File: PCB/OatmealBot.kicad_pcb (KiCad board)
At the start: 2 copper layers, 65 x 56 mm, 43 parts, among them J1 4, J10 3, J11 6, J12 7, J2 RPi_GPIO, J3 5, J4 1, J5 3, J6 4, J7 2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

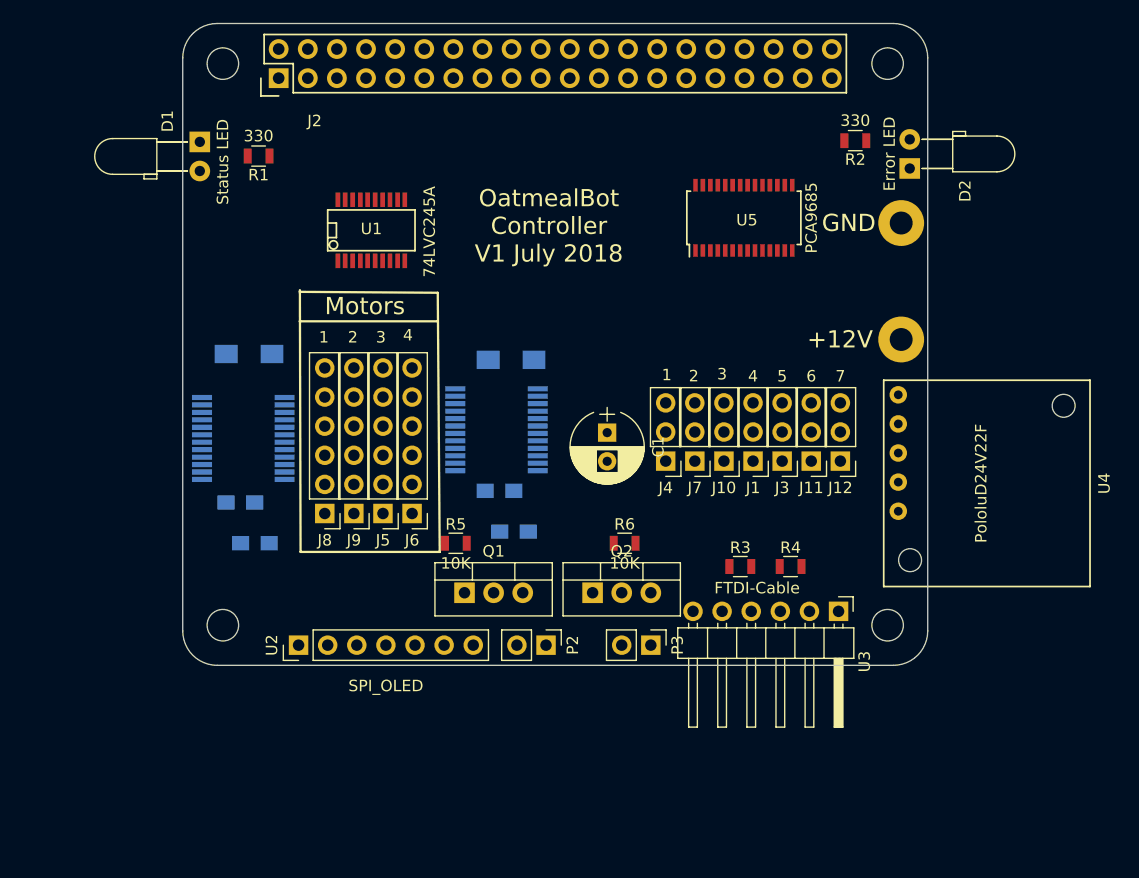
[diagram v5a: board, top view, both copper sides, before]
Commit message: PCB layout changes
Move things around to make the high power tracks shorter
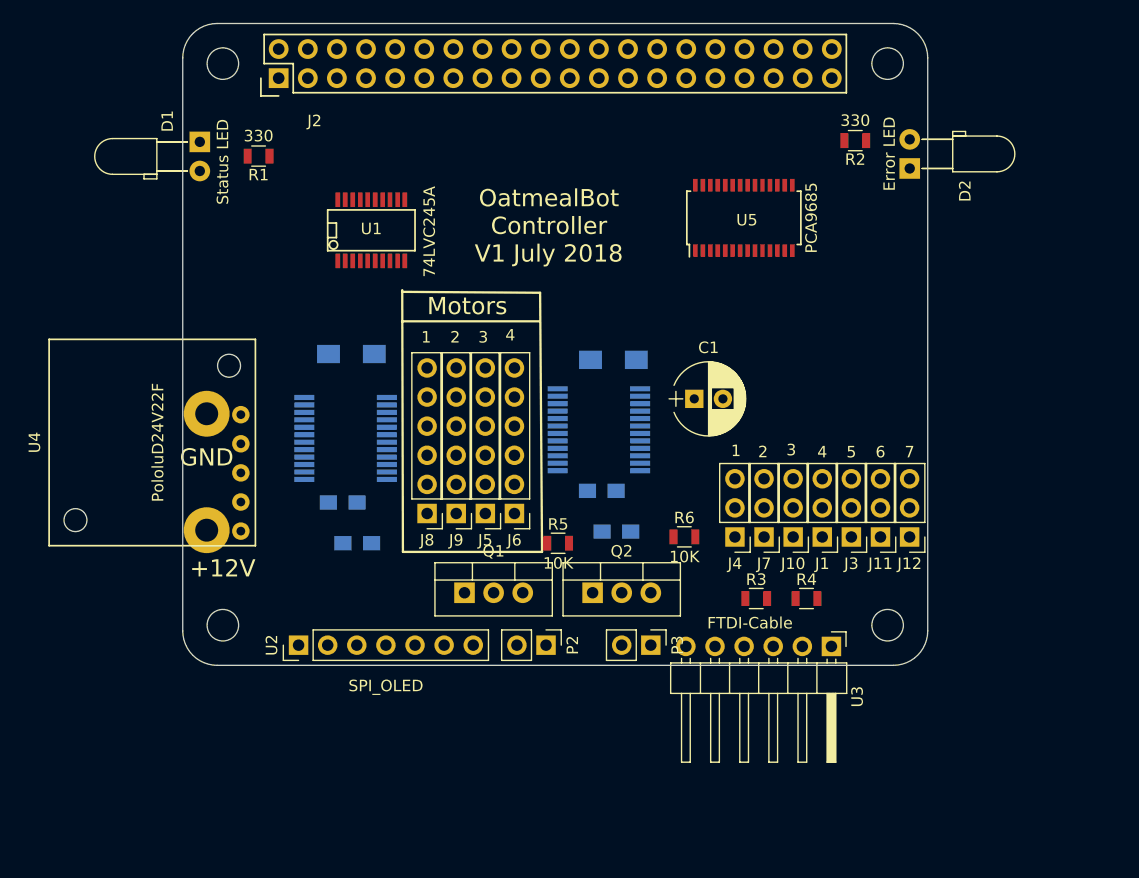
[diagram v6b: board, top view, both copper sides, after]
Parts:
- moved U4 72.9 mm to (9.84, 61.1), turned to 270 degrees
- moved P1 62.8 mm to (14.6, 58.5)
- moved J11 8.96 mm to (73.4, 69.3)
- moved J12 8.96 mm to (75.9, 69.3)
- moved J7 8.96 mm to (63.2, 69.3)
- moved J1 8.96 mm to (68.3, 69.3)
- moved J4 8.96 mm to (60.7, 69.3)
- moved J10 8.96 mm to (65.8, 69.3)
- moved J3 8.96 mm to (70.8, 69.3)
- moved C2 8.93 mm to (27.7, 69.8)
- moved C3 8.93 mm to (27.2, 53.3)
- moved C4 8.93 mm to (50.3, 68.8)
- moved C5 8.93 mm to (49.1, 65.3)
- moved C6 8.93 mm to (50.1, 53.8)
- moved C7 8.93 mm to (26.5, 66.3)
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
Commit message: Layout refinement, better power connector
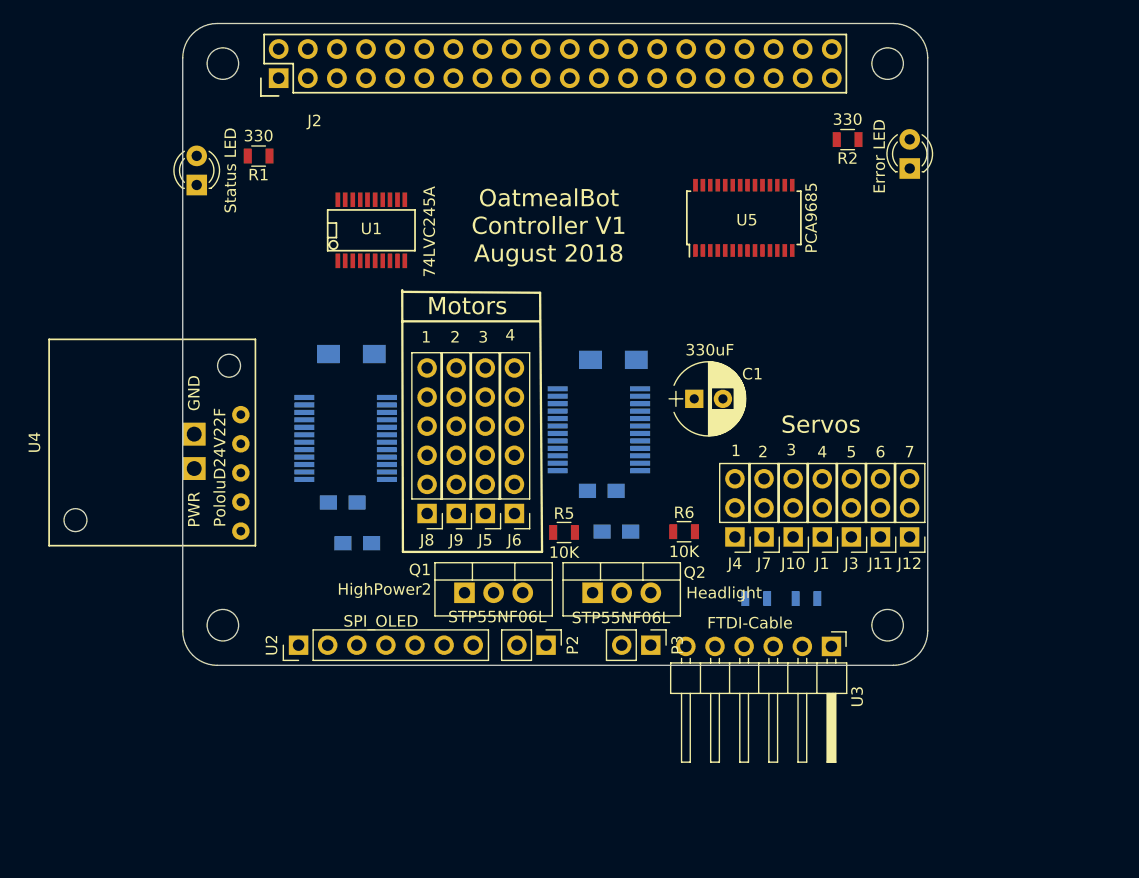
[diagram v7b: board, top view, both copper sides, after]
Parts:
- D1, D2: footprint LEDs:LED_D3.0mm_Horizontal_O3.81mm_Z10.0mm -> LEDs:LED_D3.0mm
- P1: footprint Wire_Connections_Bridges:WireConnection_2.00mmDrill -> Schminktronics:Power_Connector_Soldered
- R3, R4: moved to B.Cu
- moved D1 3.77 mm to (13.7, 38.6), turned to 90 degrees
- moved P1 3.46 mm to (13.5, 61.8), turned to 90 degrees
- moved R5 1.07 mm to (45.8, 68.9)
- moved R2 0.68 mm to (70.5, 34.6)
- moved R6 0.45 mm to (56.2, 68.8)
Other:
- board text added: "OatmealBot Controller V1 August 2018"
- board text added: "Servos"
- board text removed: "+12V"
- board text removed: "GND"
- board text removed: "OatmealBot Controller V1 July 2018"
